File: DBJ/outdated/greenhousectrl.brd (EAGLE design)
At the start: 69.5 x 80 mm, 53 parts, among them IC1 ATMEGA168TQFP-08, IC3 7805DT, IC4 L298, J1 5.5x2.1mm Barrel, K1 JQX-15F, Q1 2N3904, Y2 16MHZ

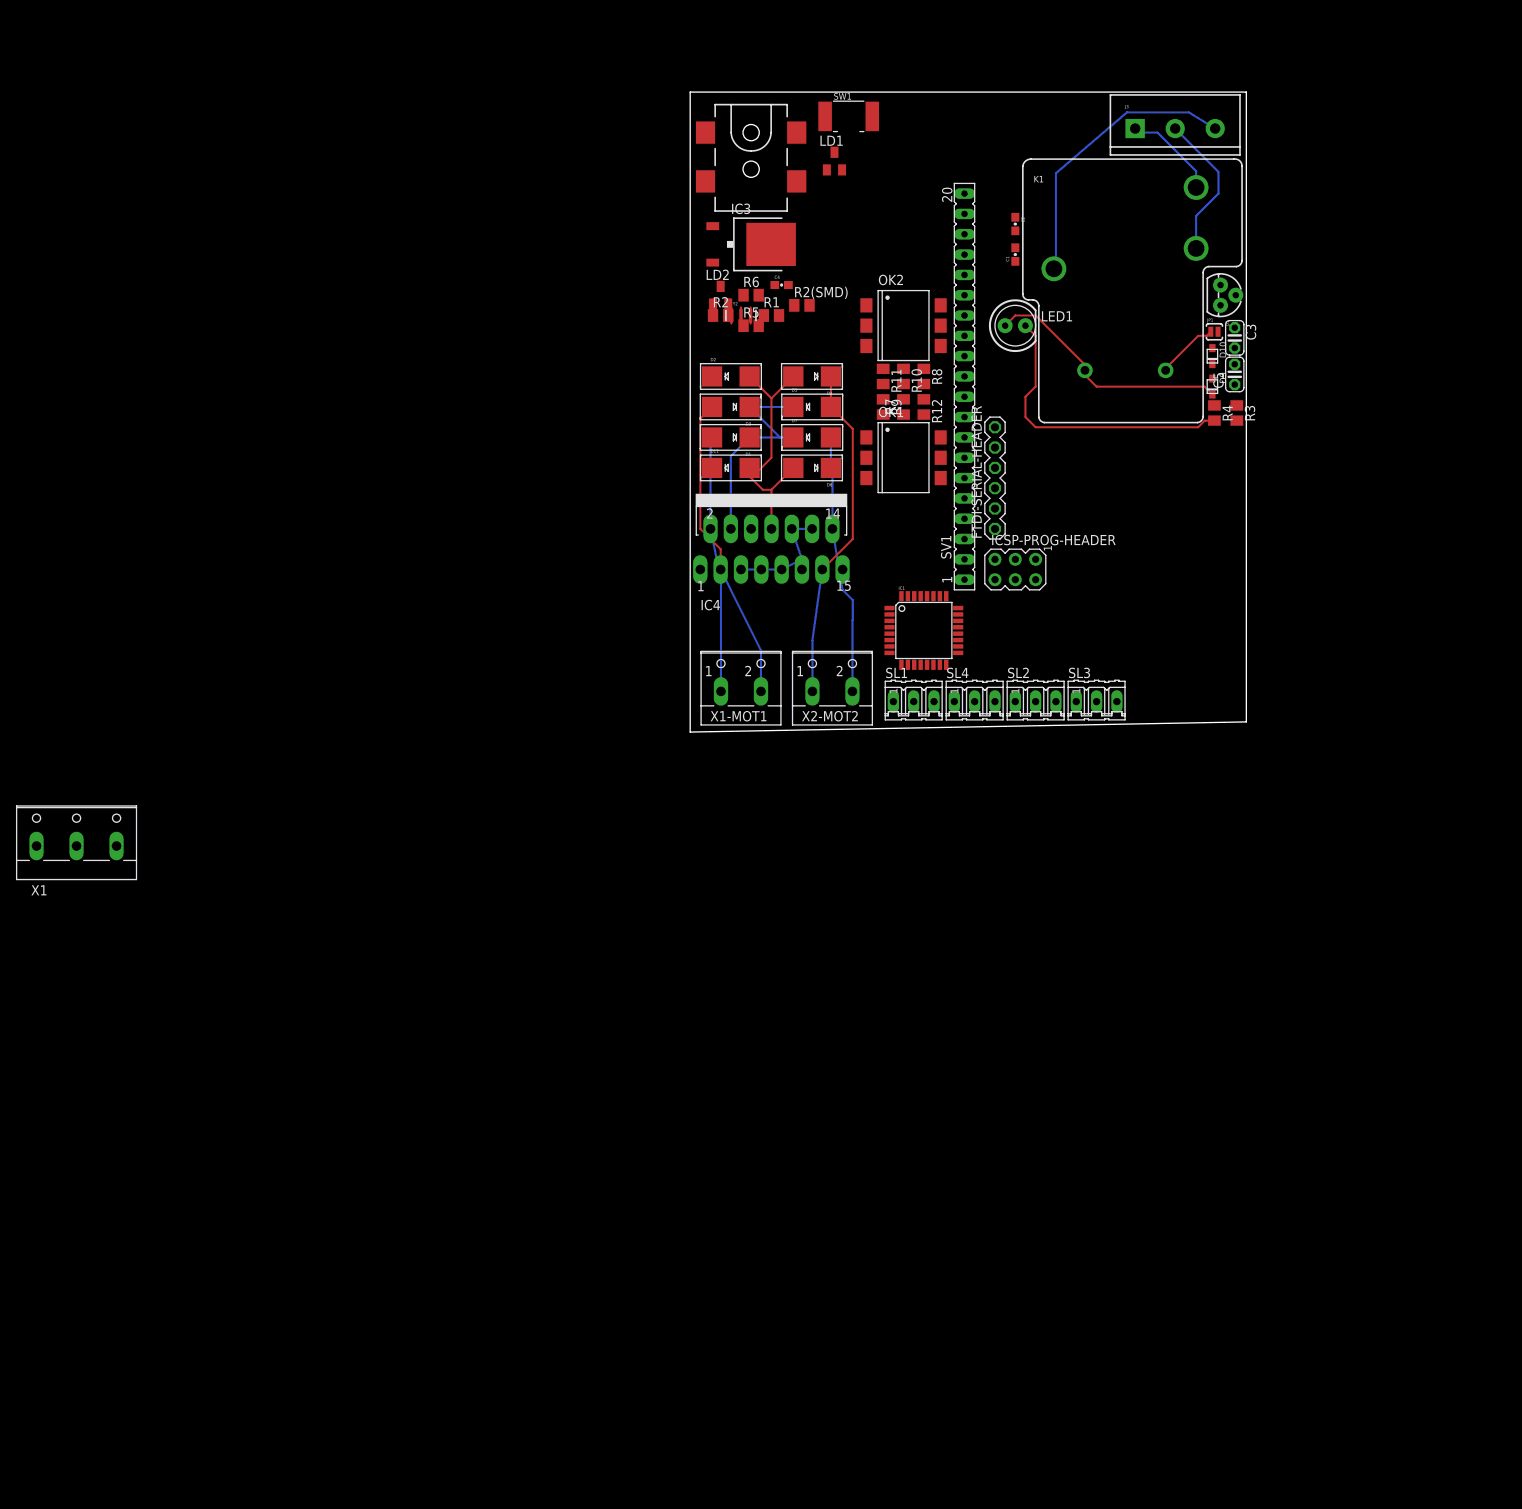
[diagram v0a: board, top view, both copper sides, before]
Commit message: Updated Schematic Notes
smaller relay, smd parts added for leds instead of thru-hole, smaller
diodes for h-bridge
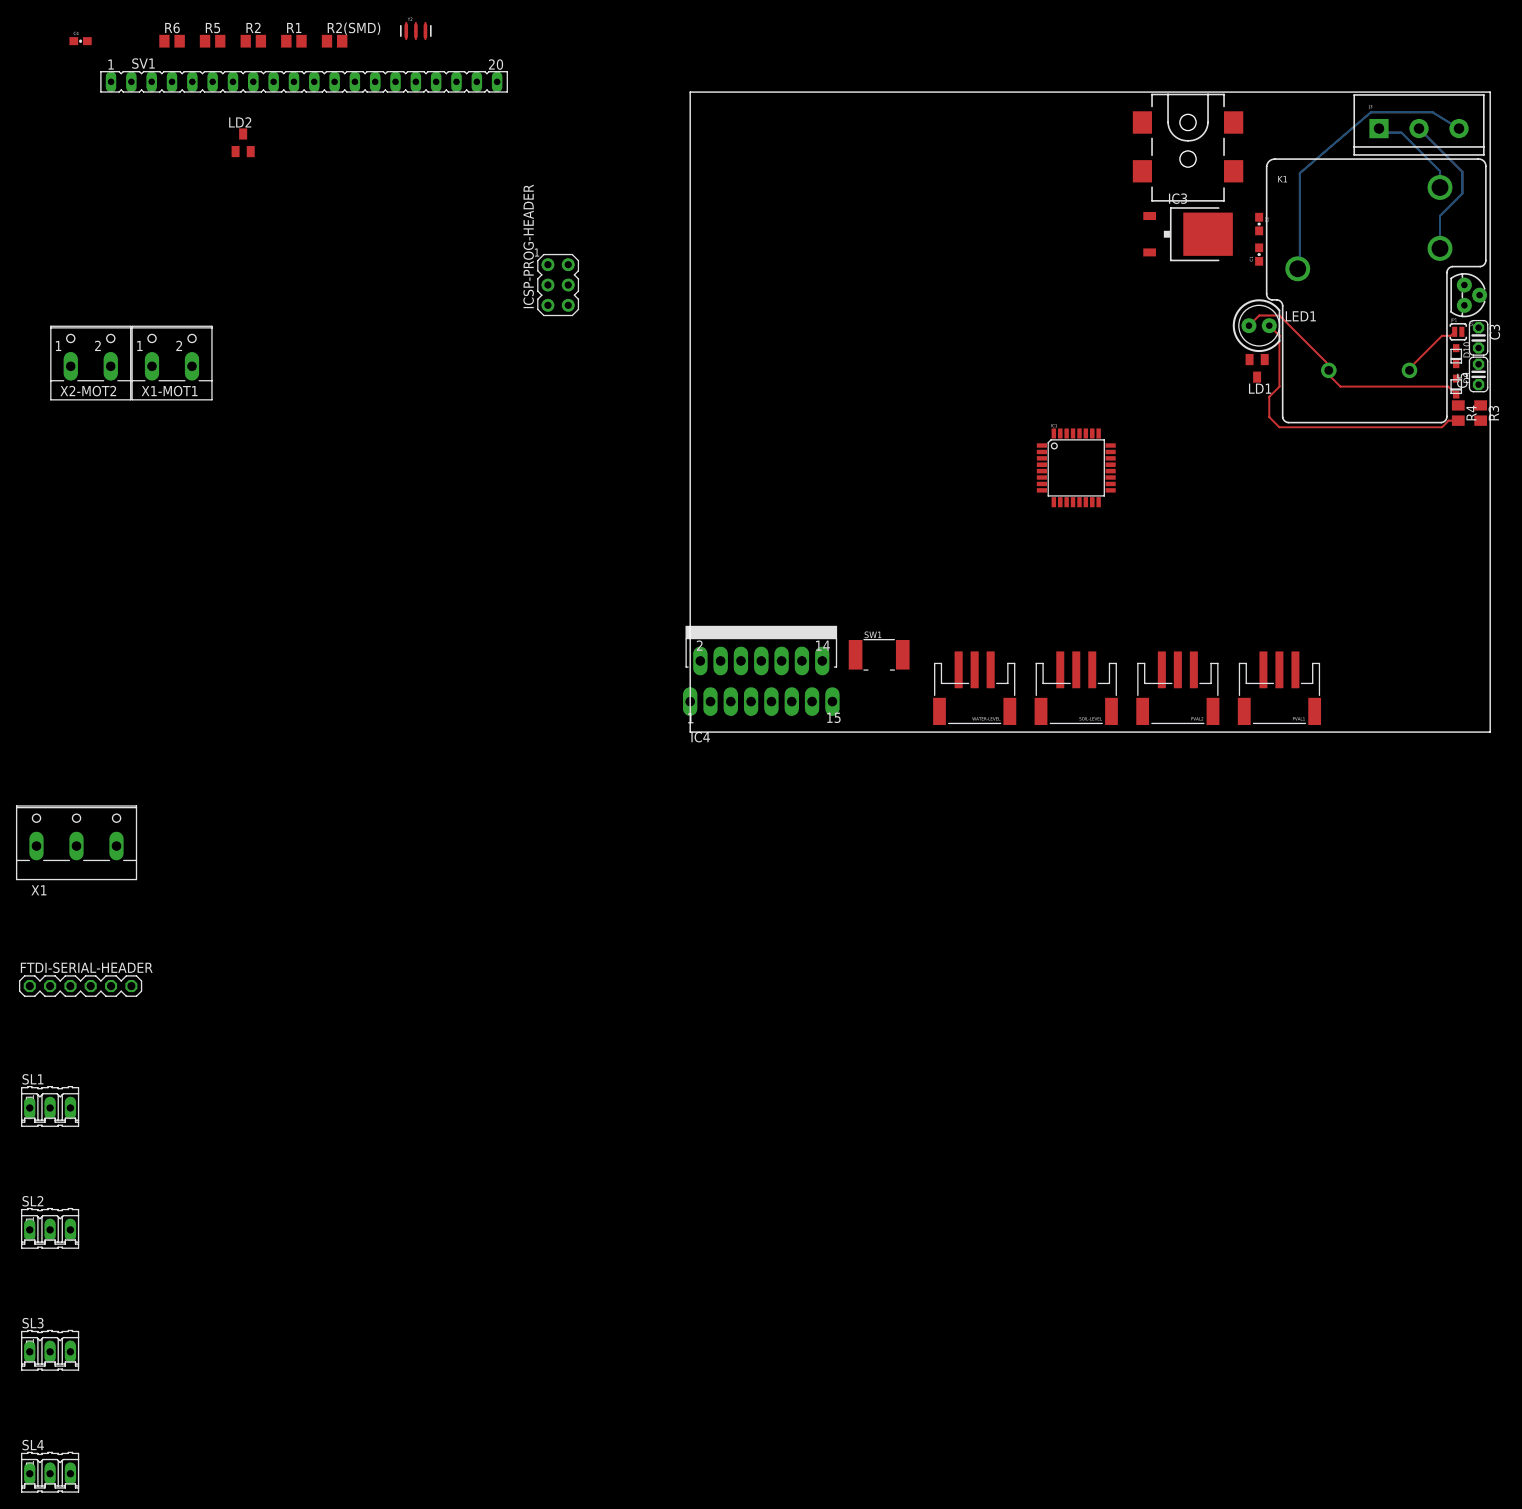
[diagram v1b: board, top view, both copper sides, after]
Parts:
- removed D1, D11, D2, D3, D4, D5, D6, D7: (no value), adafruit:SMADIODE
- removed OK1, OK2: 4N27SM, optocoupler:DIL6-SMD
- removed R10, R11, R12, R7, R8, R9: (no value), adafruit:M0805
- added PVAL1, PVAL2, SOIL-LEVEL, WATER-LEVEL: (no value), adafruit:JSTPH3
- moved SL3 154.0 mm to (-80.0, -77.5)
- moved SL4 150.6 mm to (-80.0, -92.7)
- moved SL2 139.8 mm to (-80.0, -62.2)
- moved FTDI-SERIAL-HEADER 130.8 mm to (-76.2, -31.8), turned to 0 degrees
- moved SL1 119.3 mm to (-80.0, -47.0)
- moved X2-MOT2 101.2 mm to (-74.9, 47.0)
- moved C4 92.8 mm to (-76.2, 86.4)
- moved SV1 90.9 mm to (-48.3, 81.3), turned to 0 degrees
- moved X1-MOT1 81.9 mm to (-64.8, 47.0)
- moved R6 79.0 mm to (-64.8, 86.4)
- moved R5 76.1 mm to (-59.7, 86.4)
- moved R1 68.8 mm to (-49.5, 86.4)
- moved R2 67.7 mm to (-54.6, 86.4)
- moved SW1 67.4 mm to (23.6, 9.65)
- moved ICSP-PROG-HEADER 67.3 mm to (-16.5, 55.9), turned to 0 degrees
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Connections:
- net SEN_A renamed N$13
- net SEN_B renamed N$14
- removed net ENA: IC4.6, OK2.5
- removed net ENB: IC4.11, OK1.5
- removed net N$1: OK2.1, R8.2
- removed net N$4: OK2.2, R7.2
- removed net N$5: OK2.4, R9.2
- removed net OUT1: D1.A, D11.C, IC4.2, X1-MOT1.1
- removed net OUT2: D2.C, D3.A, IC4.3, X1-MOT1.2
- removed net OUT3: D4.C, D5.A, IC4.13, X2-MOT2.1
- removed net OUT4: D6.C, D7.A, IC4.14, X2-MOT2.2
- new net N$7: IC4.2, X2-MOT2.2
- net +12V: no longer D1.C, D3.C, D5.C, D7.C
- net +5V: now also PVAL1.2, PVAL2.2, SOIL-LEVEL.2, WATER-LEVEL.2; no longer SL1.2, SL2.2, SL3.2, SL4.2
- net GND: now also PVAL1.3, PVAL2.3, SOIL-LEVEL.3, WATER-LEVEL.3; no longer D11.A, D2.A, D4.A, D6.A, OK1.6, OK2.6, R10.1, R12.1, R7.1, R9.1, SL1.1, SL2.1, SL3.1, SL4.1
- net N$15: now also IC4.3, X2-MOT2.1; no longer OK1.4, R12.2
- net N$8: now also IC4.13, X1-MOT1.2; no longer OK1.1, R11.2
- net N$9: now also IC4.14, X1-MOT1.1; no longer OK1.2, R10.2
- net PC0: now also PVAL1.1; no longer SL1.3
- net PC1: now also PVAL2.1; no longer SL2.3
- net PC2: now also SOIL-LEVEL.1; no longer SL3.3
- net PC3: now also WATER-LEVEL.1; no longer SL4.3
- net PD4: now also IC4.6; no longer R8.1
- net PD5: now also IC4.11; no longer R11.1
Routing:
- net OUT3: track 42.2 -> 0.00 mm
- net OUT2: track 38.6 -> 0.00 mm
- net OUT4: track 32.5 -> 0.00 mm
- net OUT1: track 32.2 -> 0.00 mm
- net GND: track 30.6 -> 0.00 mm
- net +12V: track 28.7 -> 0.00 mm
- net +5V: track 14.5 -> 0.00 mm
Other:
- board size 69.5 x 80 mm -> 100 x 80 mm
